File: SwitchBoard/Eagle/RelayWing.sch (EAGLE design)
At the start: 29 parts, among them K1 EE2-3TNUH, K2 EE2-3TNUH, K3 EE2-3TNUH, K4 EE2-3TNUH, K5 EE2-3TNUH, U1 ULN2003ANSR, U2 ULN2003ANSR, U3 MCP23017SS, U4 INA219AID

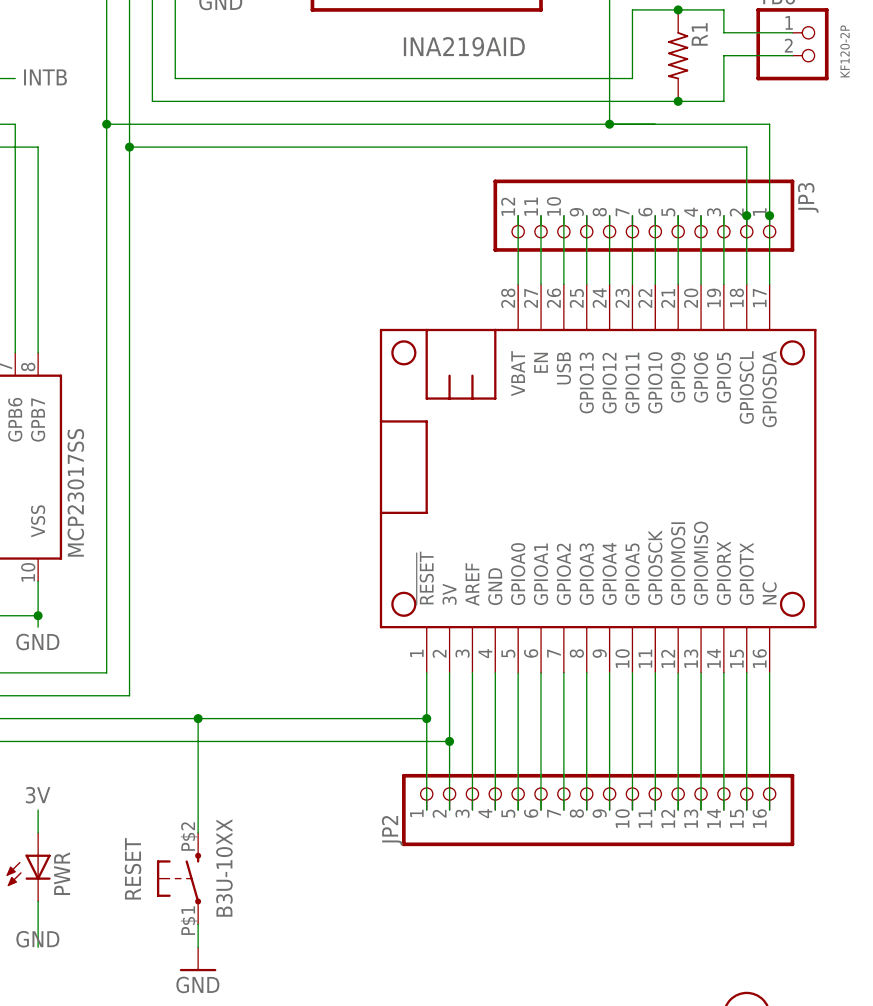
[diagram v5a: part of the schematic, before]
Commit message: tinker with 5pin header
relay drivers on brd need to be checked, RN1 moved. Ground plated mounting hole(s).
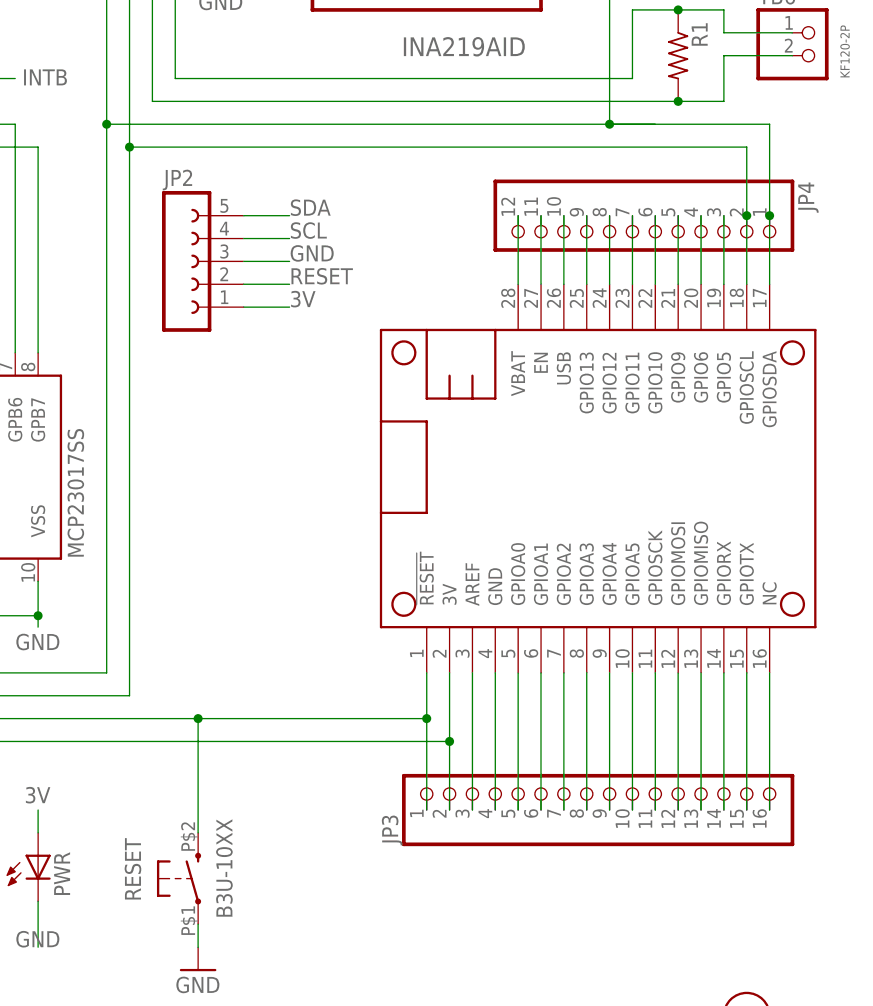
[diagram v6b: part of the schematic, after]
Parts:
- added JP4: (no value), pinhead:PINHD-1X12
- JP2: device pinhead:PINHD-1X16 -> con-lsta:FE05W
- JP3: device pinhead:PINHD-1X12 -> pinhead:PINHD-1X16
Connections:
- removed net N$18: JP2.1, MS1.!RESET, RESET.S, U3.!RESET
- new net RESET: JP2.2, JP3.1, MS1.!RESET, RESET.S, U3.!RESET
- net 3V: now also JP2.1, JP3.2; no longer JP2.2
- net GND: now also JP2.3, JP3.4; no longer JP2.4
- net N$1: now also JP3.3; no longer JP2.3
- net N$10: now also JP3.12; no longer JP2.12
- net N$11: now also JP3.13; no longer JP2.13
- net N$12: now also JP3.14; no longer JP2.14
- net N$13: now also JP3.15; no longer JP2.15
- net N$14: now also JP3.16; no longer JP2.16
- net N$15: now also JP4.3; no longer JP3.3
- net N$19: now also JP4.4; no longer JP3.4
- net N$20: now also JP4.5; no longer JP3.5
- net N$21: now also JP4.6; no longer JP3.6
- net N$22: now also JP4.7; no longer JP3.7
- net N$23: now also JP4.8; no longer JP3.8
- net N$3: now also JP3.5; no longer JP2.5
- net N$4: now also JP3.6; no longer JP2.6
- net N$5: now also JP3.7; no longer JP2.7
- net N$51: now also JP4.9; no longer JP3.9
- net N$6: now also JP3.8; no longer JP2.8
- net N$61: now also JP4.11; no longer JP3.11
- net N$7: now also JP3.9; no longer JP2.9
- net N$8: now also JP3.10; no longer JP2.10
- net N$9: now also JP3.11; no longer JP2.11
- net SCL: now also JP2.4, JP4.2; no longer JP3.2
- net SDA: now also JP2.5, JP4.1; no longer JP3.1
- net USB: now also JP4.10; no longer JP3.10
- net VBAT: now also JP4.12; no longer JP3.12

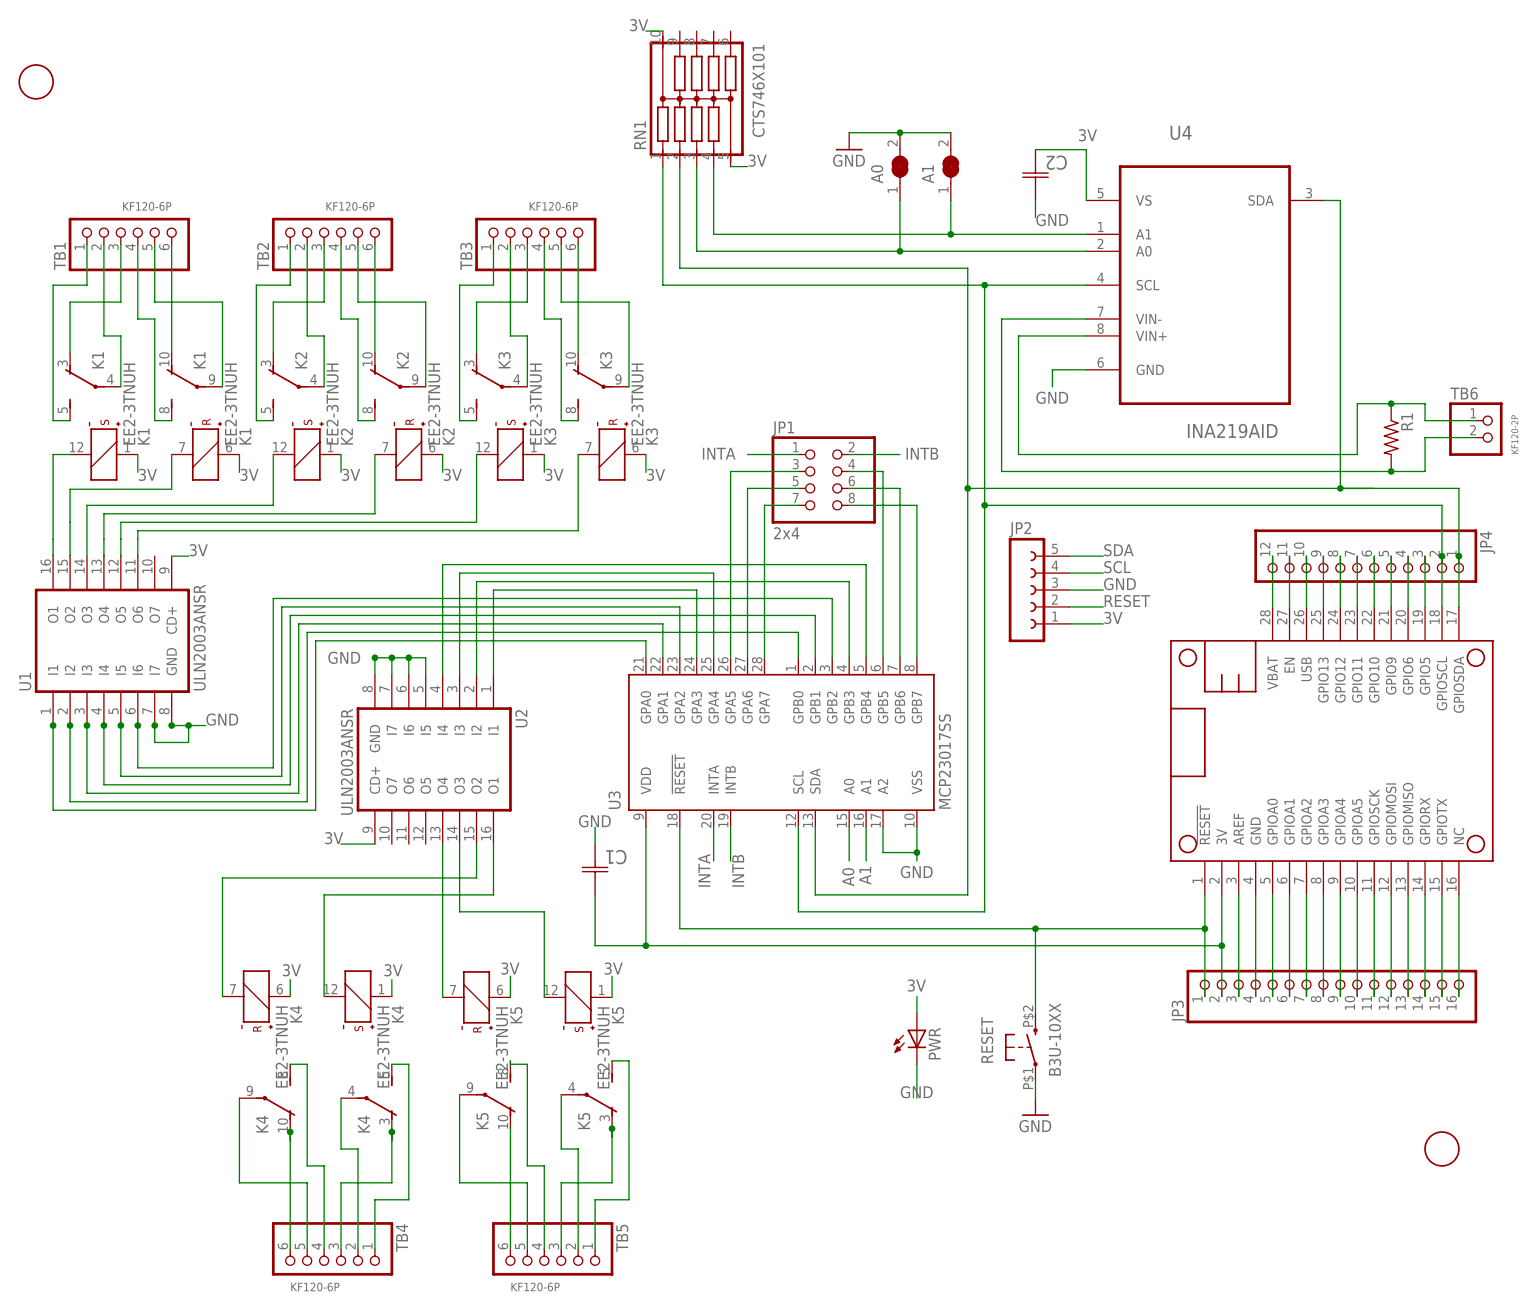
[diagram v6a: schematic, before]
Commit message: sch: RN GPIO radius fixes brd: no airwires
This reverts to my May 17 sch file which fixed the resistor network part and GPIO signals followed by Bill's May 26 routed brd file.
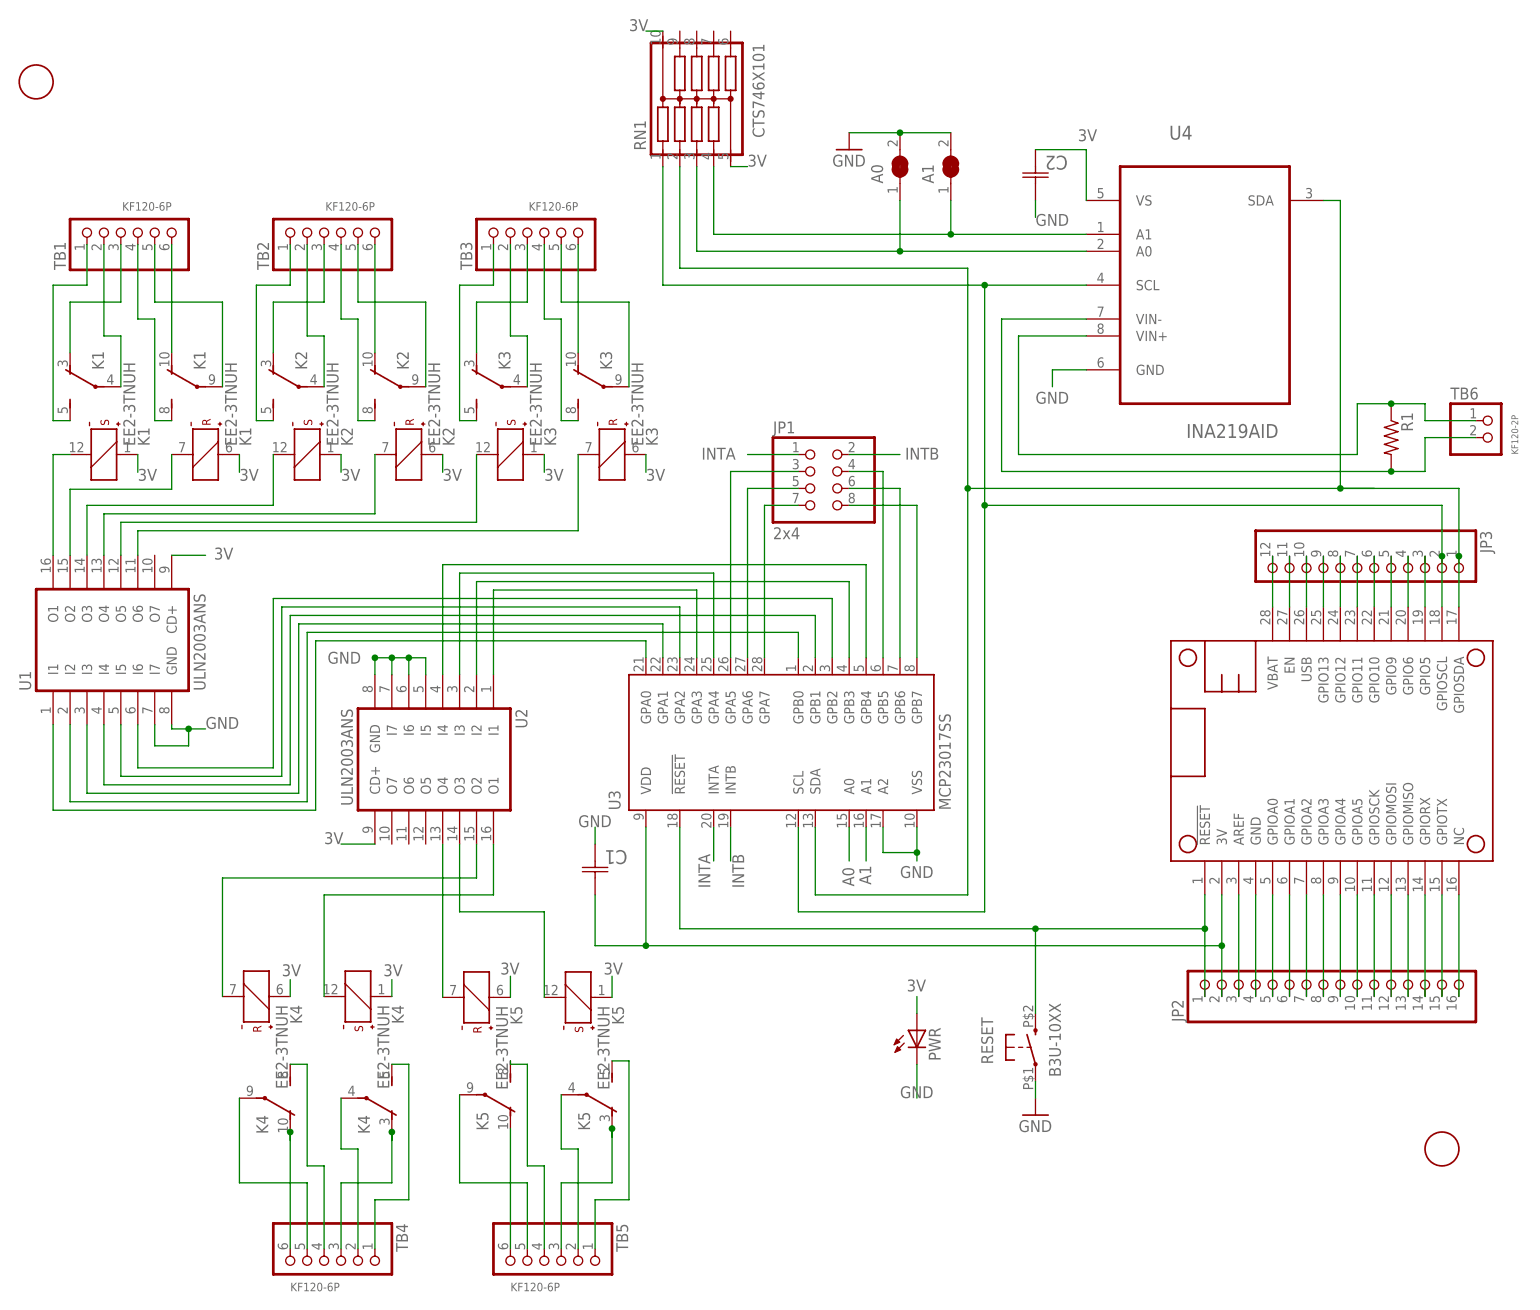
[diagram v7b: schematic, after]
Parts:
- removed JP4: (no value), pinhead:PINHD-1X12
- JP2: device con-lsta:FE05W -> pinhead:PINHD-1X16
- JP3: device pinhead:PINHD-1X16 -> pinhead:PINHD-1X12
- U1, U2: value ULN2003ANSR -> ULN2003ANS; device home:ULN2003ANSR -> home:ULN2003ANS
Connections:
- removed net RESET: JP2.2, JP3.1, MS1.!RESET, RESET.S, U3.!RESET
- new net N$18: JP2.1, MS1.!RESET, RESET.S, U3.!RESET
- net 3V: now also JP2.2; no longer JP2.1, JP3.2
- net GND: now also JP2.4; no longer JP2.3, JP3.4
- net N$1: now also JP2.3; no longer JP3.3
- net N$10: now also JP2.12; no longer JP3.12
- net N$11: now also JP2.13; no longer JP3.13
- net N$12: now also JP2.14; no longer JP3.14
- net N$13: now also JP2.15; no longer JP3.15
- net N$14: now also JP2.16; no longer JP3.16
- net N$15: now also JP3.3; no longer JP4.3
- net N$19: now also JP3.4; no longer JP4.4
- net N$20: now also JP3.5; no longer JP4.5
- net N$21: now also JP3.6; no longer JP4.6
- net N$22: now also JP3.7; no longer JP4.7
- net N$23: now also JP3.8; no longer JP4.8
- net N$3: now also JP2.5; no longer JP3.5
- net N$4: now also JP2.6; no longer JP3.6
- net N$5: now also JP2.7; no longer JP3.7
- net N$51: now also JP3.9; no longer JP4.9
- net N$6: now also JP2.8; no longer JP3.8
- net N$61: now also JP3.11; no longer JP4.11
- net N$7: now also JP2.9; no longer JP3.9
- net N$8: now also JP2.10; no longer JP3.10
- net N$9: now also JP2.11; no longer JP3.11
- net SCL: now also JP3.2; no longer JP2.4, JP4.2
- net SDA: now also JP3.1; no longer JP2.5, JP4.1
- net USB: now also JP3.10; no longer JP4.10
- net VBAT: now also JP3.12; no longer JP4.12

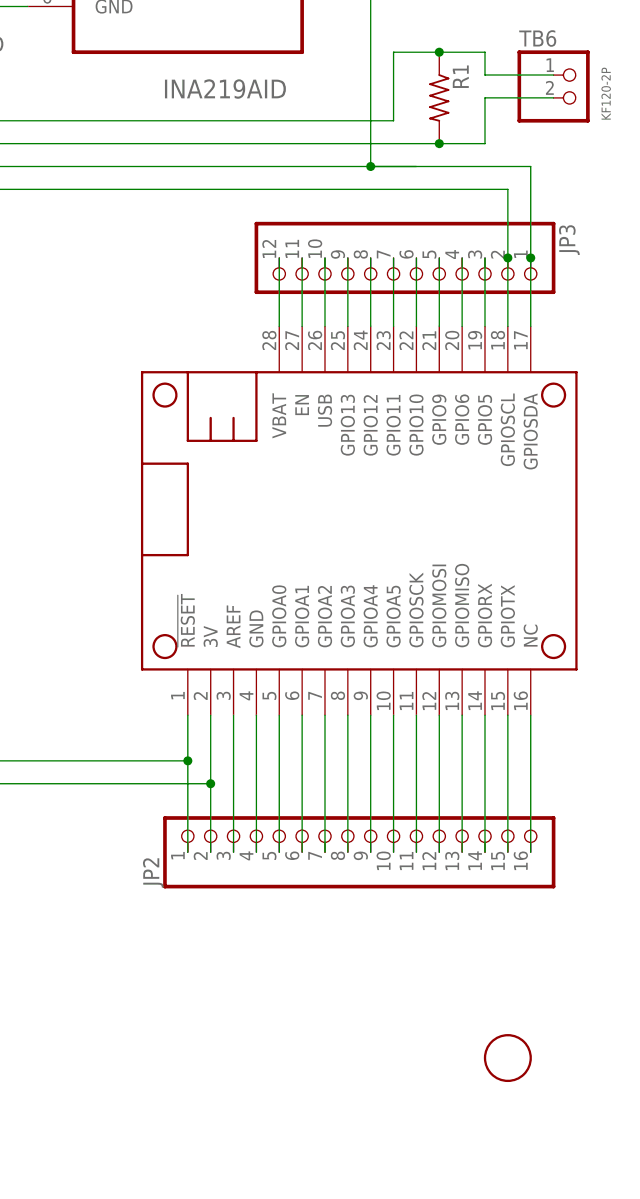
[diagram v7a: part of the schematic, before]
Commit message: Added 4-pin 12c header (no silkscreen changes yet)
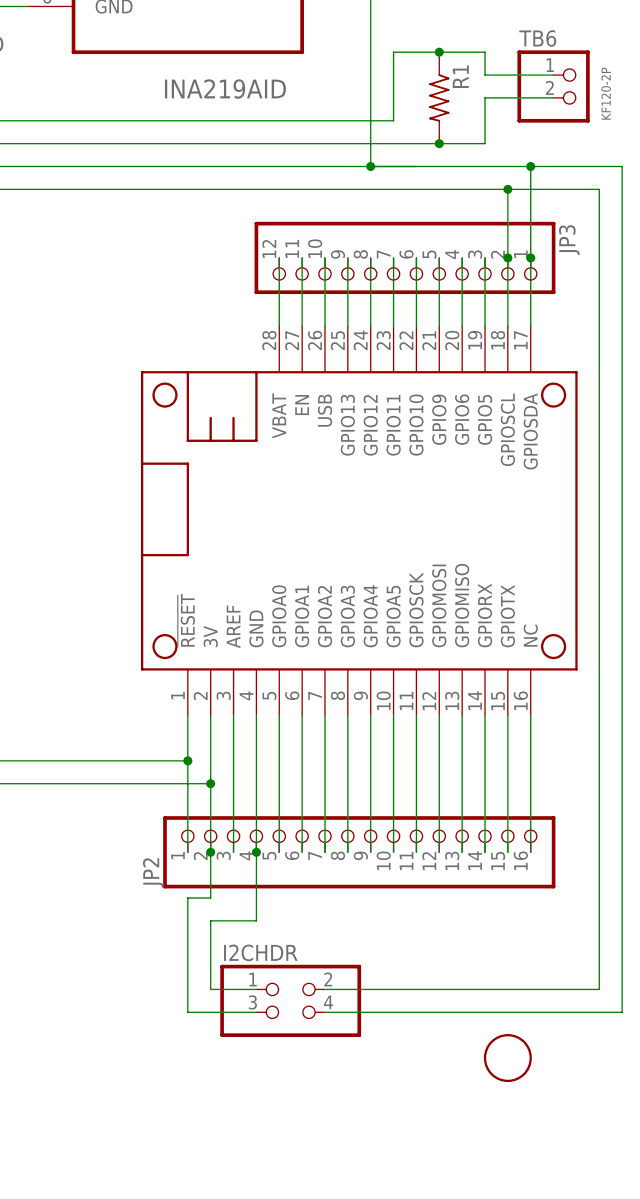
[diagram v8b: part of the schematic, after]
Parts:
- added I2CHDR: (no value), pinhead:PINHD-2X2
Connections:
- net 3V: now also I2CHDR.3
- net GND: now also I2CHDR.1
- net SCL: now also I2CHDR.2
- net SDA: now also I2CHDR.4
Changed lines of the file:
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@@
 <?xml version="1.0" encoding="utf-8"?>
 <!DOCTYPE eagle SYSTEM "eagle.dtd">
-<eagle version="8.6.3">
+<eagle version="9.0.1">
 <drawing>
 <settings>
-<setting alwaysvectorfont="yes"/>
+<setting alwaysvectorfont="no"/>
 <setting keepoldvectorfont="yes"/>
 <setting verticaltext="up"/>
@@
 <part name="RN1" library="home" deviceset="CTS746X101" device=""/>
 <part name="RESET" library="home" deviceset="B3U-10XX" device=""/>
+<part name="I2CHDR" library="pinhead" library_urn="urn:adsk.eagle:library:325" deviceset="PINHD-2X2" device="" package3d_urn="urn:adsk.eagle:package:22455/2" value=" "/>
 </parts>
 <sheets>
@@
 <attribute name="VALUE" x="176.53" y="46.355" size="1.778" layer="96" rot="R90"/>
 </instance>
+<instance part="I2CHDR" gate="A" x="210.82" y="40.64"/>
 </instances>
 <busses>
@@
 <pinref part="JP2" gate="A" pin="4"/>
 <wire x1="205.74" y1="73.66" x2="205.74" y2="58.42" width="0.1524" layer="91"/>
+<pinref part="I2CHDR" gate="A" pin="1"/>
+<wire x1="205.74" y1="43.18" x2="200.66" y2="43.18" width="0.1524" layer="91"/>
+<wire x1="200.66" y1="43.18" x2="200.66" y2="50.8" width="0.1524" layer="91"/>
+<wire x1="200.66" y1="50.8" x2="205.74" y2="50.8" width="0.1524" layer="91"/>
+<wire x1="205.74" y1="50.8" x2="205.74" y2="58.42" width="0.1524" layer="91"/>
+<junction x="205.74" y="58.42"/>
 </segment>
 </net>
@@
 <wire x1="200.66" y1="66.04" x2="200.66" y2="58.42" width="0.1524" layer="91"/>
 <junction x="200.66" y="66.04"/>
+<wire x1="200.66" y1="58.42" x2="200.66" y2="53.34" width="0.1524" layer="91"/>
+<junction x="200.66" y="58.42"/>
+<wire x1="200.66" y1="53.34" x2="198.12" y2="53.34" width="0.1524" layer="91"/>
+<pinref part="I2CHDR" gate="A" pin="3"/>
+<wire x1="198.12" y1="53.34" x2="198.12" y2="40.64" width="0.1524" layer="91"/>
+<wire x1="198.12" y1="40.64" x2="205.74" y2="40.64" width="0.1524" layer="91"/>
 </segment>
 <segment>
@@
 <pinref part="RN1" gate="G$1" pin="1"/>
 <junction x="165.1" y="165.1"/>
+<pinref part="I2CHDR" gate="A" pin="2"/>
+<wire x1="213.36" y1="43.18" x2="243.84" y2="43.18" width="0.1524" layer="91"/>
+<wire x1="243.84" y1="43.18" x2="243.84" y2="132.08" width="0.1524" layer="91"/>
+<wire x1="243.84" y1="132.08" x2="233.68" y2="132.08" width="0.1524" layer="91"/>
+<junction x="233.68" y="132.08"/>
 </segment>
 </net>
@@
 <pinref part="RN1" gate="G$1" pin="2"/>
 <junction x="162.56" y="134.62"/>
+<pinref part="I2CHDR" gate="A" pin="4"/>
+<wire x1="213.36" y1="40.64" x2="246.38" y2="40.64" width="0.1524" layer="91"/>
+<wire x1="246.38" y1="40.64" x2="246.38" y2="134.62" width="0.1524" layer="91"/>
+<wire x1="246.38" y1="134.62" x2="236.22" y2="134.62" width="0.1524" layer="91"/>
+<junction x="236.22" y="134.62"/>
 </segment>
 </net>
